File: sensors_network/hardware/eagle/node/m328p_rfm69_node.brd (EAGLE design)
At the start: 65.5 x 39.9 mm, 32 parts, among them IC2 L6920, U1 M328P, U2 RFM69W, Y1 8MHz

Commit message: [sensors_network] added 10K pull-up resistor for ICSP interference
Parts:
- added R3: 10K, SparkFun-Resistors:0805
- moved SJ2 1.30 mm to (19.1, 20.6)
- moved C9 0.76 mm to (18.3, 15.5)
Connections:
- net +3V3: now also R3.2
- net SS: now also R3.1
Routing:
- net SS: track 13.2 -> 17.4 mm
- net N$7: track 24.4 -> 23.3 mm
- net +3V3: track 176.7 -> 177.8 mm

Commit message: [sensors_network] pcb final touches
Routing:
- net N$7: track 23.3 -> 22.2 mm
- net GND: track 217.6 -> 218.4 mm
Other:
- outline, holes or cut-outs redrawn
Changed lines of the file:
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@@
 <board>
 <plain>
-<wire x1="65.766" y1="0" x2="65.766" y2="39.802" width="0" layer="20"/>
-<wire x1="65.766" y1="39.802" x2="0.254" y2="39.802" width="0" layer="20"/>
 <hole x="2.286" y="37.846" drill="3"/>
 <hole x="2.286" y="2.032" drill="3"/>
 <hole x="63.754" y="2.032" drill="3"/>
 <hole x="63.754" y="37.846" drill="3"/>
-<wire x1="0.762" y1="39.878" x2="65.786" y2="39.878" width="0.3048" layer="20"/>
-<wire x1="65.786" y1="39.878" x2="65.786" y2="1.016" width="0.3048" layer="20"/>
-<wire x1="65.786" y1="1.016" x2="65.766" y2="0" width="0.3048" layer="20"/>
+<wire x1="0.254" y1="39.878" x2="65.786" y2="39.878" width="0.3048" layer="20"/>
+<wire x1="65.786" y1="39.878" x2="65.786" y2="0" width="0.3048" layer="20"/>
 <wire x1="65.766" y1="0" x2="0.254" y2="0" width="0.3048" layer="20"/>
 <wire x1="0.254" y1="0" x2="0.254" y2="39.802" width="0.3048" layer="20"/>
-<wire x1="0.254" y1="39.802" x2="0.762" y2="39.878" width="0.3048" layer="20"/>
 <text x="5.842" y="25.146" size="0.8128" layer="21">VB_EN | VB_DIS</text>
 <text x="17.272" y="18.542" size="0.8128" layer="21">VB_EN</text>
@@
 <wire x1="28.956" y1="31.242" x2="37.338" y2="31.242" width="0.4064" layer="1"/>
 <wire x1="37.338" y1="31.242" x2="37.592" y2="30.988" width="0.4064" layer="1"/>
-<wire x1="14.041" y1="21.442" x2="14.041" y2="19.558" width="0.4064" layer="1"/>
+<wire x1="14.041" y1="21.442" x2="14.041" y2="19.304" width="0.4064" layer="1"/>
 <wire x1="8.762" y1="22.606" x2="9.27" y2="20.448" width="0.4064" layer="1"/>
-<wire x1="9.27" y1="20.448" x2="10.16" y2="19.558" width="0.4064" layer="1"/>
-<wire x1="10.16" y1="19.558" x2="11.43" y2="19.558" width="0.4064" layer="1"/>
-<wire x1="11.43" y1="19.558" x2="14.041" y2="19.558" width="0.4064" layer="1"/>
-<wire x1="11.43" y1="12.192" x2="11.43" y2="19.558" width="0.4064" layer="1"/>
+<wire x1="9.27" y1="20.448" x2="10.16" y2="19.304" width="0.4064" layer="1"/>
+<wire x1="10.16" y1="19.304" x2="11.43" y2="19.304" width="0.4064" layer="1"/>
+<wire x1="11.43" y1="19.304" x2="14.041" y2="19.304" width="0.4064" layer="1"/>
+<wire x1="11.43" y1="12.192" x2="11.43" y2="19.304" width="0.4064" layer="1"/>
 <wire x1="23.23" y1="13.208" x2="23.23" y2="13.462" width="0.4064" layer="1"/>
-<wire x1="23.23" y1="13.462" x2="21.59" y2="15.102" width="0.4064" layer="1"/>
+<wire x1="23.23" y1="13.462" x2="22.918" y2="13.774" width="0.4064" layer="1"/>
 <wire x1="40.778" y1="12.954" x2="47.498" y2="12.954" width="0.4064" layer="1"/>
 <wire x1="47.498" y1="12.954" x2="57.912" y2="12.954" width="0.4064" layer="1"/>
@@
 <wire x1="13.716" y1="12.308" x2="15.99" y2="12.308" width="0.4064" layer="1"/>
 <wire x1="15.99" y1="12.308" x2="18.288" y2="13.844" width="0.4064" layer="1"/>
-<wire x1="18.288" y1="13.844" x2="21.094" y2="14.606" width="0.4064" layer="1"/>
-<wire x1="21.094" y1="14.606" x2="21.59" y2="15.102" width="0.4064" layer="1"/>
-<polygon width="0.4064" layer="1" isolate="0.4064" thermals="no">
-<vertex x="0.254" y="39.878"/>
-<vertex x="65.786" y="39.878"/>
-<vertex x="65.786" y="0"/>
-<vertex x="0.254" y="0"/>
-</polygon>
 <wire x1="23.368" y1="9.398" x2="20.066" y2="6.096" width="0.4064" layer="1"/>
 <wire x1="23.368" y1="9.398" x2="23.368" y2="11.038" width="0.4064" layer="1"/>
@@
 <wire x1="29.464" y1="34.036" x2="29.464" y2="31.75" width="0.4064" layer="1"/>
 <wire x1="29.464" y1="31.75" x2="28.956" y2="31.242" width="0.4064" layer="1"/>
+<wire x1="18.288" y1="13.844" x2="21.844" y2="13.844" width="0.4064" layer="1"/>
+<wire x1="21.844" y1="13.844" x2="22.918" y2="13.844" width="0.4064" layer="1"/>
+<wire x1="22.918" y1="13.844" x2="22.918" y2="13.774" width="0.4064" layer="1"/>
+<wire x1="21.59" y1="15.102" x2="21.59" y2="14.098" width="0.4064" layer="1"/>
+<wire x1="21.59" y1="14.098" x2="21.844" y2="13.844" width="0.4064" layer="1"/>
+<polygon width="0.4064" layer="1" isolate="0.4064" thermals="no">
+<vertex x="0.254" y="39.878"/>
+<vertex x="65.786" y="39.878"/>
+<vertex x="65.786" y="0"/>
+<vertex x="0.254" y="0"/>
+</polygon>
 </signal>
 <signal name="MOSI">
@@
 <wire x1="50.038" y1="22.998" x2="49.9" y2="22.86" width="0.4064" layer="1"/>
 <wire x1="25.03" y1="13.208" x2="25.03" y2="16.88" width="0.6096" layer="1"/>
-<wire x1="25.03" y1="16.88" x2="19.812" y2="20.574" width="0.6096" layer="1"/>
 <wire x1="4.572" y1="6.096" x2="3.048" y2="7.62" width="0.6096" layer="1"/>
 <wire x1="3.048" y1="7.62" x2="3.048" y2="31.496" width="0.6096" layer="1"/>
@@
 <wire x1="19.42" y1="23.622" x2="19.812" y2="22.976" width="0.6096" layer="1"/>
 <wire x1="19.812" y1="22.976" x2="19.812" y2="20.574" width="0.6096" layer="1"/>
+<wire x1="25.03" y1="16.88" x2="21.336" y2="20.574" width="0.6096" layer="1"/>
+<wire x1="21.336" y1="20.574" x2="19.812" y2="20.574" width="0.6096" layer="1"/>
 </signal>
 <signal name="N$1">
 <contactref element="IC2" pad="7"/>
 <contactref element="L1" pad="P$1"/>
-<wire x1="11.176" y1="20.574" x2="11.43" y2="20.32" width="0.4064" layer="1"/>
-<wire x1="11.43" y1="20.32" x2="13.208" y2="20.32" width="0.4064" layer="1"/>
-<wire x1="13.391" y1="21.442" x2="13.391" y2="20.503" width="0.4064" layer="1"/>
-<wire x1="13.391" y1="20.503" x2="13.208" y2="20.32" width="0.4064" layer="1"/>
+<wire x1="11.176" y1="20.574" x2="11.43" y2="20.32" width="0.6096" layer="1"/>
+<wire x1="11.43" y1="20.32" x2="13.208" y2="20.32" width="0.6096" layer="1"/>
 <wire x1="9.398" y1="16.51" x2="9.398" y2="15.264" width="0.4064" layer="1"/>
 <wire x1="9.398" y1="15.264" x2="8.612" y2="16.256" width="0.4064" layer="1"/>
@@
 <wire x1="10.16" y1="25.146" x2="11.176" y2="24.13" width="0.6096" layer="1"/>
 <wire x1="11.176" y1="24.13" x2="11.176" y2="20.574" width="0.6096" layer="1"/>
+<wire x1="13.391" y1="21.442" x2="13.391" y2="20.32" width="0.4064" layer="1"/>
+<wire x1="13.391" y1="20.32" x2="13.208" y2="20.32" width="0.4064" layer="1"/>
 </signal>
 <signal name="N$4">
@@
 <contactref element="IC2" pad="5"/>
 <contactref element="SJ2" pad="1"/>
-<wire x1="12.741" y1="21.442" x2="12.741" y2="22.647" width="0.4064" layer="1"/>
 <wire x1="12.741" y1="15.642" x2="12.741" y2="16.805" width="0.4064" layer="1"/>
 <wire x1="21.59" y1="16.902" x2="19.292" y2="16.902" width="0.4572" layer="1"/>
 <wire x1="19.292" y1="16.902" x2="18.288" y2="17.144" width="0.4572" layer="1"/>
-<wire x1="14.691" y1="21.442" x2="14.691" y2="23.073" width="0.4064" layer="1"/>
-<wire x1="14.691" y1="23.073" x2="14.732" y2="23.114" width="0.4064" layer="1"/>
-<wire x1="13.208" y1="23.114" x2="12.741" y2="22.647" width="0.4572" layer="1"/>
-<wire x1="13.208" y1="23.114" x2="14.65" y2="23.114" width="0.4572" layer="1"/>
-<wire x1="14.65" y1="23.114" x2="14.691" y2="23.073" width="0.4572" layer="1"/>
 <wire x1="12.741" y1="16.805" x2="13.08" y2="17.144" width="0.4064" layer="1"/>
 <wire x1="13.08" y1="17.144" x2="18.288" y2="17.144" width="0.4064" layer="1"/>
-<wire x1="18.288" y1="20.574" x2="15.748" y2="23.114" width="0.4572" layer="1"/>
-<wire x1="15.748" y1="23.114" x2="14.732" y2="23.114" width="0.4572" layer="1"/>
 <wire x1="18.288" y1="20.574" x2="18.288" y2="17.144" width="0.4572" layer="1"/>
+<wire x1="12.741" y1="21.442" x2="12.741" y2="22.393" width="0.4064" layer="1"/>
+<wire x1="12.741" y1="22.393" x2="12.954" y2="22.606" width="0.4572" layer="1"/>
+<wire x1="12.954" y1="22.606" x2="14.732" y2="22.606" width="0.4572" layer="1"/>
+<wire x1="14.732" y1="22.606" x2="15.748" y2="22.606" width="0.4572" layer="1"/>
+<wire x1="14.691" y1="21.442" x2="14.691" y2="22.565" width="0.4064" layer="1"/>
+<wire x1="14.691" y1="22.565" x2="14.732" y2="22.606" width="0.4064" layer="1"/>
+<wire x1="18.288" y1="20.574" x2="17.78" y2="20.574" width="0.4572" layer="1"/>
+<wire x1="17.78" y1="20.574" x2="15.748" y2="22.606" width="0.4572" layer="1"/>
 </signal>
 <signal name="SDA">

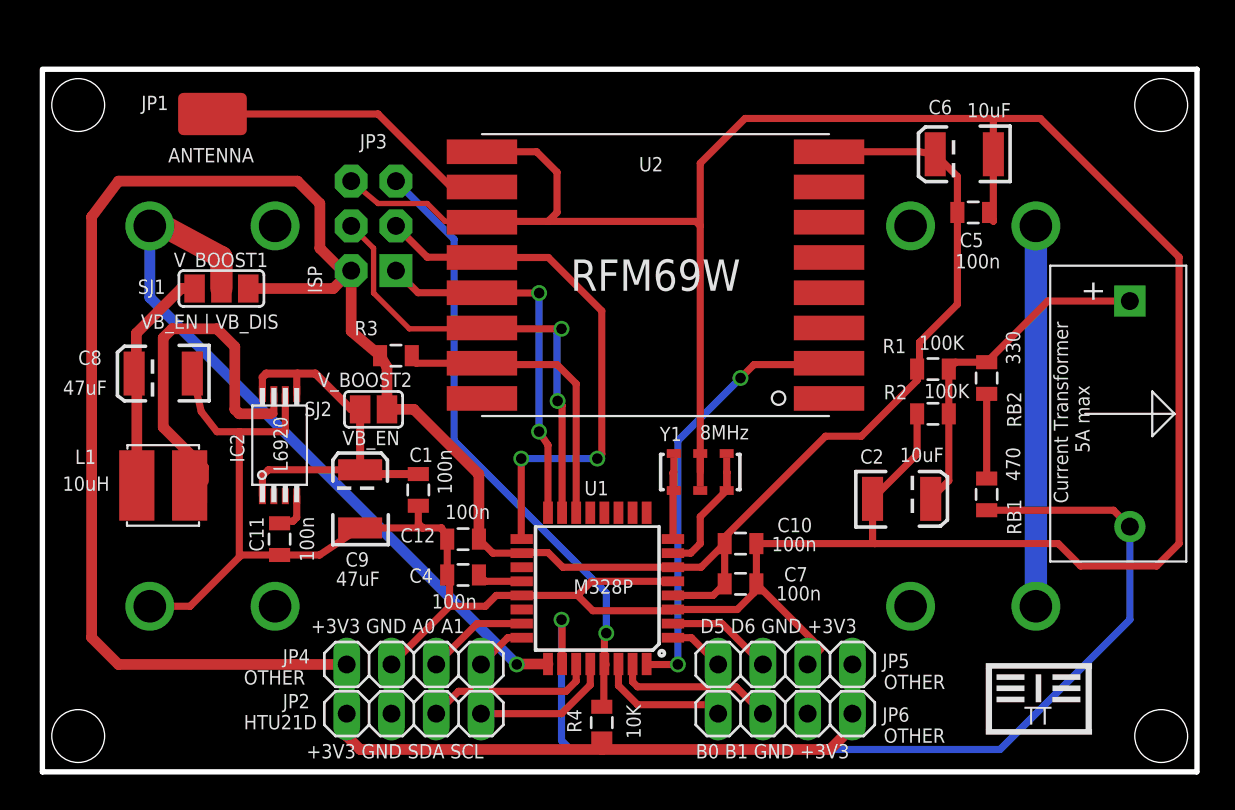
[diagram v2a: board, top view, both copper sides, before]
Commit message: [sensors_network] pcb - added node id config switch and activity led
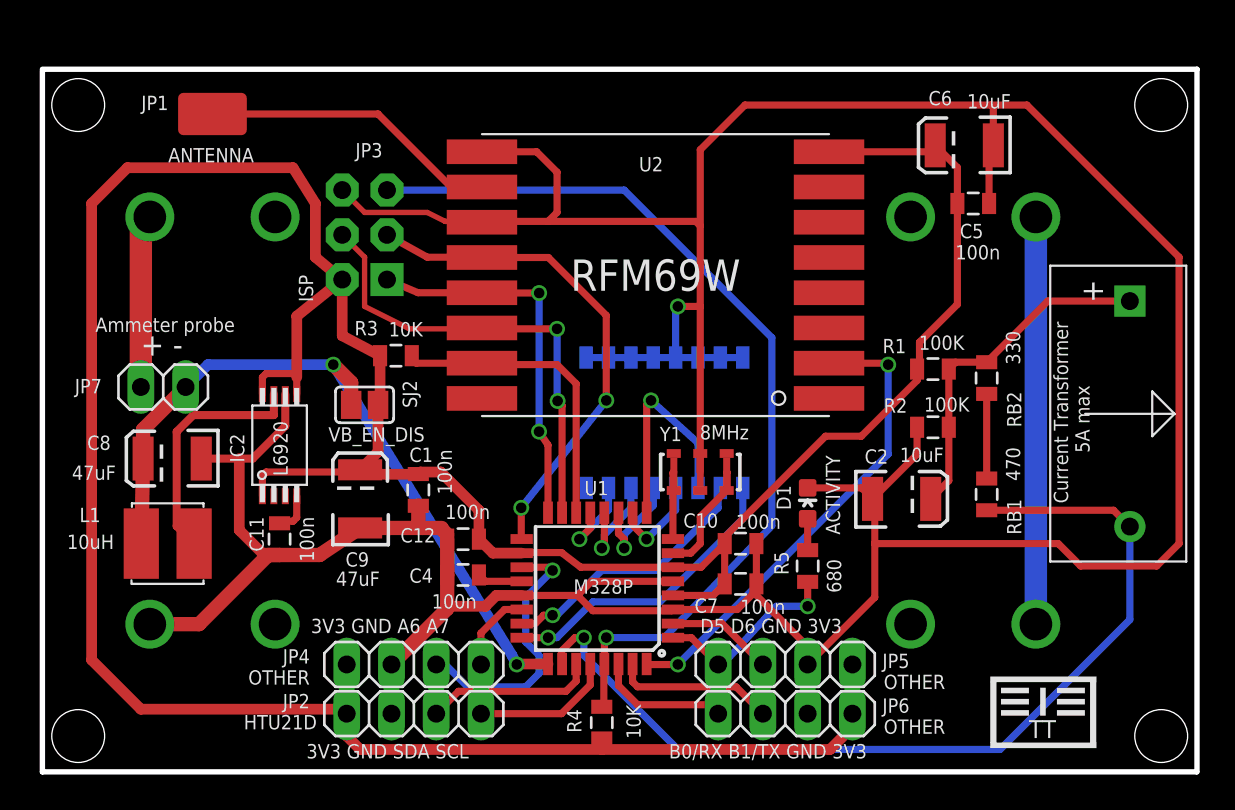
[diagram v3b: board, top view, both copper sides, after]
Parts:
- removed SJ1: V_BOOST1, jumper:SJ_2
- added D1: ACTIVITY, SparkFun-LED:LED-0603
- added JP7: Ammeter probe, pinhead:1X02
- added R5: 680, SparkFun-Passives:0805
- added SW2: Node ID, SparkFun-Electromechanical:DIPSWITCH-08-50MIL
- SJ2: value V_BOOST2 -> VB_EN_DIS
- moved C8 4.85 mm to (7.62, 17.8)
- moved L1 3.31 mm to (7.37, 13.0)
- moved BAT4 1.02 mm to (31.5, 8.38)
- moved R2 0.76 mm to (50.8, 19.6)
- moved JP3 0.72 mm to (18.5, 30.5)
- moved SJ2 0.57 mm to (18.5, 20.8), turned to 180 degrees
- moved C5 0.51 mm to (53.1, 32.3)
- moved C6 0.51 mm to (52.6, 35.6)
- moved BAT3 0.51 mm to (31.5, 31.5)
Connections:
- removed net A0: JP4.3, U1.23
- removed net A1: JP4.4, U1.24
- removed net N$7: C1.1, C9.A, IC2.1, IC2.5, IC2.8, SJ2.1
- new net A6: JP4.3, U1.19
- new net A7: JP4.4, U1.22
- new net C0: SW2.2, U1.23
- new net C1: SW2.1, U1.24
- new net C2: SW2.3, U1.9
- new net C3: SW2.4, U1.10
- new net C4: SW2.5, U1.11
- new net C5: SW2.6, U1.12
- new net C6: SW2.7, U1.13
- new net N$5: BAT3.PWR@1, JP7.2
- net +3V3: now also C1.1, C9.A, IC2.1, IC2.5, IC2.8, SJ2.1; no longer SJ1.1, SJ2.2
- net BATT_LVL: now also C8.A, JP7.1, L1.P$2, SJ2.2; no longer BAT3.PWR@1, SJ1.2
- net D5: now also R5.1
- net GND: now also D1.C, SW2.10, SW2.11, SW2.12, SW2.13, SW2.14, SW2.15, SW2.16, SW2.9
- net N$2: now also D1.A, R5.2; no longer C8.A, L1.P$2, SJ1.3
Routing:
- net N$7: track 22.2 -> 0.00 mm
- net +3V3: track 178.2 -> 196.3 mm
- net C1: track 0.00 -> 17.1 mm, vias 0 -> 1
- net RESET: track 35.0 -> 52.1 mm
- net C0: track 0.00 -> 15.8 mm, vias 0 -> 1
- net GND: track 218.4 -> 233.9 mm, vias 0 -> 1
- net A6: track 0.00 -> 15.3 mm, vias 0 -> 1
- net C2: track 0.00 -> 12.6 mm, vias 0 -> 1
- net N$2: track 14.4 -> 1.78 mm
- net N$5: track 0.00 -> 9.86 mm
- net N$1: track 23.3 -> 13.9 mm
- net D5: track 3.19 -> 11.1 mm, vias 0 -> 1
- net C4: track 0.00 -> 6.24 mm, vias 0 -> 1
- net C5: track 0.00 -> 6.16 mm, vias 0 -> 1
- net A0: track 5.81 -> 0.00 mm
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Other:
- board text added: "+ -"
- board text added: "3V3 GND A6 A7"
- board text added: "3V3 GND SDA SCL"
- board text added: "B0/RX B1/TX GND 3V3"
- board text added: "D5 D6 GND 3V3"
- board text removed: "+3V3 GND A0 A1"
- board text removed: "+3V3 GND SDA SCL"
- board text removed: "B0 B1 GND +3V3"
- board text removed: "D5 D6 GND +3V3"
- board text removed: "VB_EN"
- board text removed: "VB_EN | VB_DIS"

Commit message: [sensors_network] pcb - moved battery holders outside a little bit to make more room for the node id config switch
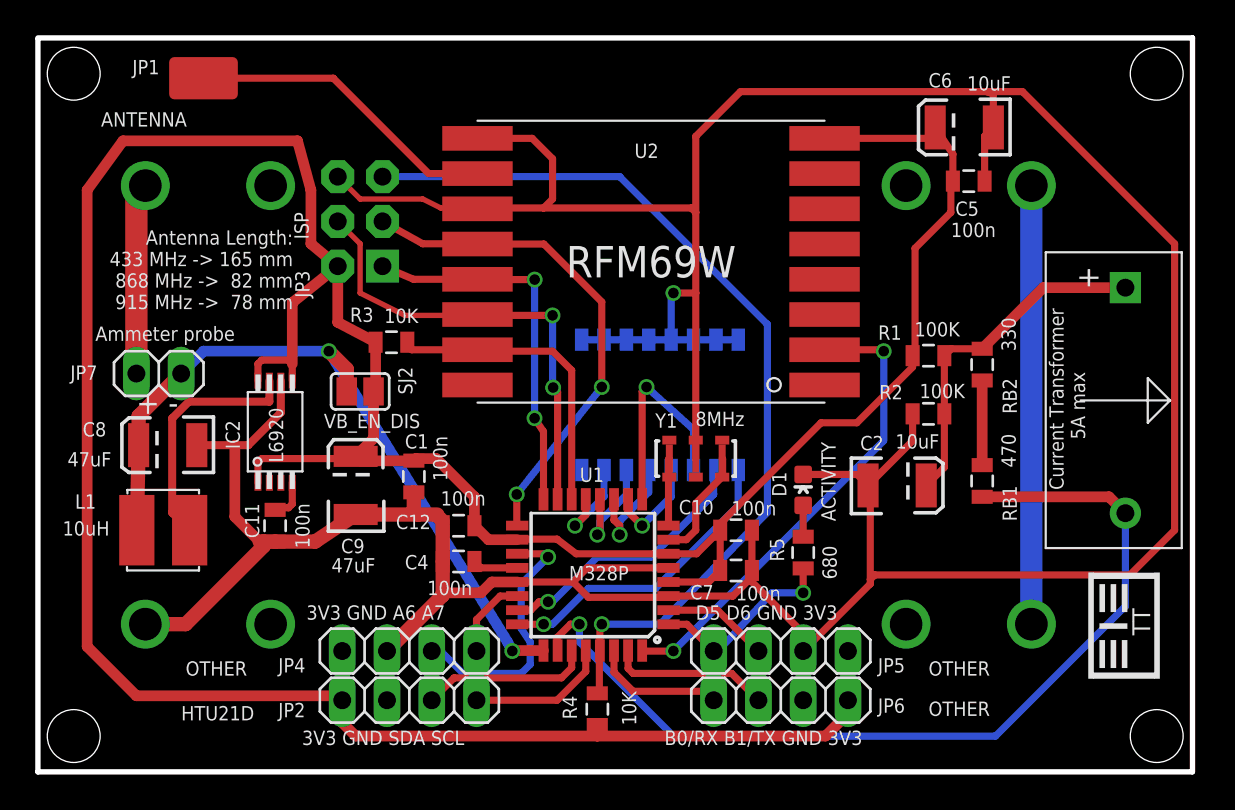
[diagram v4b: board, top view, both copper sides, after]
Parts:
- moved JP1 2.09 mm to (9.40, 39.4)
- moved BAT3 1.80 mm to (31.2, 33.3)
- moved C5 1.30 mm to (52.8, 33.5)
- moved SW2 1.05 mm to (35.3, 20.8)
- moved C6 1.02 mm to (52.6, 36.6)
- moved R5 0.80 mm to (43.4, 12.4)
- moved RB1 0.80 mm to (53.6, 16.5)
- moved C1 0.80 mm to (21.3, 16.8)
- moved C9 0.80 mm to (18.0, 16.3)
- moved JP3 0.80 mm to (18.3, 31.2)
- moved R3 0.80 mm to (20.1, 24.4)
- moved SJ2 0.80 mm to (18.3, 21.6)
- moved U1 0.80 mm to (31.5, 11.2)
- moved C8 0.80 mm to (7.37, 18.5)
- moved JP7 0.80 mm to (6.86, 22.6)
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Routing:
- net +3V3: track 196.3 -> 198.4 mm
- net N$8: track 23.1 -> 24.9 mm
- net N$5: track 9.86 -> 10.9 mm
- net N$10: track 17.0 -> 17.8 mm
- net GND: track 233.9 -> 233.4 mm
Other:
- board size 65.5 x 39.9 mm -> 65.5 x 41.7 mm
